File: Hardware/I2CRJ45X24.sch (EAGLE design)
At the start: 127 parts, among them IC1 MCP23017SO, IC2 MCP23017SO, IC3 MCP23017SO, IC4 MCP23017SO, IC5 MCP23017SO, IC6 MCP23017SO, J1 RJ45-X8, J2 RJ45-X8, J3 RJ45-X8, J4 I2C-BREAKOUT, J5 M01-PLAIN, J9 I2C-BREAKOUT

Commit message: Renumbered parts to optimise production.
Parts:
- removed J9: I2C-BREAKOUT, SuperHouse-Connectors:M02X3-SHROUDED
- added J6: M01-PLAIN, SuperHouse-Connectors:M01-PLAIN
- J5: value M01-PLAIN -> I2C-BREAKOUT; device SuperHouse-Connectors:M01-PLAIN -> SuperHouse-Connectors:M02X3-SHROUDED
- R100, R99: value 1K -> 4K7
- R68, R69: value 4K7 -> 1K
- renumbered LED3 to LED1, R101 to R67
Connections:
- net !INT: now also J6.1; no longer J5.1
- net !RESET: now also J5.6; no longer J9.6
- net 3D1: now also R68.2; no longer R100.2
- net 3H2: now also R69.2; no longer R99.2
- net GND: now also J5.4; no longer J9.4
- net GPB0-6: now also R68.1; no longer R100.1
- net GPB5-6: now also R69.1; no longer R99.1
- net N$1: now also R99.2; no longer R68.2
- net N$2: now also R100.2; no longer R69.2
- net SCL: now also J5.1, R99.1; no longer J9.1, R68.1
- net SDA: now also J5.2, R100.1; no longer J9.2, R69.1
- net VCC: now also J5.5; no longer J9.5
- net VIN: now also J5.3; no longer J9.3
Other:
- note added: "24-Channel I2C RJ45 Breakout"
- note added: "V2.2 (2021-04-14)"
- note removed: "24 Channel I2C RJ45 Breakout"
- note removed: "V2.2 (2021-04-08)"

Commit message: Major clean-up in preparation for recreating x8 and x16 versions based on the x24 version. Moved rear silkscreen into left third. Increased size of all data traces. Improved bottom power plane pour. Changed LED resistors to 4K7.
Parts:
- J1, J2: value RJ45-X8 -> I2C-BREAKOUT; device SuperHouse-Connectors:RJ45-X8 -> SuperHouse-Connectors:M02X3-SHROUDED
- J3: value RJ45-X8 -> M01-PLAIN; device SuperHouse-Connectors:RJ45-X8 -> SuperHouse-Connectors:M01-PLAIN
- J4, J5: value I2C-BREAKOUT -> RJ45-X8; device SuperHouse-Connectors:M02X3-SHROUDED -> SuperHouse-Connectors:RJ45-X8
- J6: value M01-PLAIN -> RJ45-X8; device SuperHouse-Connectors:M01-PLAIN -> SuperHouse-Connectors:RJ45-X8
- R39, R40: value 2K2 -> 1K
- R97, R98: value 1K -> 4K7
- renumbered SJ3 to SJ1
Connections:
- net !INT: now also J3.1; no longer J6.1
- net !RESET: now also J1.6, J2.6; no longer J4.6, J5.6
- net 1A1: now also J4.A1; no longer J1.A1
- net 1A2: now also J4.A2; no longer J1.A2
- net 1A3: now also J4.A3; no longer J1.A3
- net 1A6: now also J4.A6; no longer J1.A6
- net 1B1: now also J4.B1; no longer J1.B1
- net 1B2: now also J4.B2; no longer J1.B2
- net 1B3: now also J4.B3; no longer J1.B3
- net 1B6: now also J4.B6; no longer J1.B6
- net 1C1: now also J4.C1; no longer J1.C1
- net 1C2: now also J4.C2; no longer J1.C2
- net 1C3: now also J4.C3; no longer J1.C3
- net 1C6: now also J4.C6; no longer J1.C6
- net 1D1: now also J4.D1; no longer J1.D1
- net 1D2: now also J4.D2; no longer J1.D2
- net 1D3: now also J4.D3; no longer J1.D3
- net 1D6: now also J4.D6; no longer J1.D6
- net 1E1: now also J4.E1; no longer J1.E1
- net 1E2: now also J4.E2; no longer J1.E2
- net 1E3: now also J4.E3; no longer J1.E3
- net 1E6: now also J4.E6; no longer J1.E6
- net 1F1: now also J4.F1; no longer J1.F1
- net 1F2: now also J4.F2; no longer J1.F2
- net 1F3: now also J4.F3; no longer J1.F3
- net 1F6: now also J4.F6; no longer J1.F6
- net 1G1: now also J4.G1; no longer J1.G1
- net 1G2: now also J4.G2; no longer J1.G2
- net 1G3: now also J4.G3; no longer J1.G3
- net 1G6: now also J4.G6; no longer J1.G6
- net 1H1: now also J4.H1; no longer J1.H1
- net 1H2: now also J4.H2; no longer J1.H2
- net 1H3: now also J4.H3; no longer J1.H3
- net 1H6: now also J4.H6; no longer J1.H6
- net 2A1: now also J5.A1; no longer J2.A1
- net 2A2: now also J5.A2; no longer J2.A2
- net 2A3: now also J5.A3; no longer J2.A3
- net 2A6: now also J5.A6; no longer J2.A6
- net 2B1: now also J5.B1; no longer J2.B1
- net 2B2: now also J5.B2; no longer J2.B2
- net 2B3: now also J5.B3; no longer J2.B3
- net 2B6: now also J5.B6; no longer J2.B6
- net 2C1: now also J5.C1; no longer J2.C1
- net 2C2: now also J5.C2; no longer J2.C2
- net 2C3: now also J5.C3; no longer J2.C3
- net 2C6: now also J5.C6; no longer J2.C6
- net 2D1: now also J5.D1; no longer J2.D1
- net 2D2: now also J5.D2; no longer J2.D2
- net 2D3: now also J5.D3; no longer J2.D3
- net 2D6: now also J5.D6; no longer J2.D6
- net 2E1: now also J5.E1; no longer J2.E1
- net 2E2: now also J5.E2; no longer J2.E2
- net 2E3: now also J5.E3; no longer J2.E3
- net 2E6: now also J5.E6; no longer J2.E6
- net 2F1: now also J5.F1; no longer J2.F1
- net 2F2: now also J5.F2; no longer J2.F2
- net 2F3: now also J5.F3; no longer J2.F3
- net 2F6: now also J5.F6; no longer J2.F6
- net 2G1: now also J5.G1; no longer J2.G1
- net 2G2: now also J5.G2; no longer J2.G2
- net 2G3: now also J5.G3; no longer J2.G3
- net 2G6: now also J5.G6; no longer J2.G6
- net 2H1: now also J5.H1; no longer J2.H1
- net 2H2: now also J5.H2; no longer J2.H2
- net 2H3: now also J5.H3; no longer J2.H3
- net 2H6: now also J5.H6; no longer J2.H6
- net 3A1: now also J6.A1; no longer J3.A1
- net 3A2: now also J6.A2; no longer J3.A2
- net 3A3: now also J6.A3; no longer J3.A3
- net 3A6: now also J6.A6; no longer J3.A6
- net 3B1: now also J6.B1; no longer J3.B1
- net 3B2: now also J6.B2; no longer J3.B2
- net 3B3: now also J6.B3; no longer J3.B3
- net 3B6: now also J6.B6; no longer J3.B6
- net 3C1: now also J6.C1; no longer J3.C1
- net 3C2: now also J6.C2; no longer J3.C2
- net 3C3: now also J6.C3; no longer J3.C3
- net 3C6: now also J6.C6; no longer J3.C6
- net 3D1: now also J6.D1; no longer J3.D1
- net 3D2: now also J6.D2, R40.2; no longer J3.D2, R98.2
- net 3D3: now also J6.D3; no longer J3.D3
- net 3D6: now also J6.D6; no longer J3.D6
- net 3E1: now also J6.E1; no longer J3.E1
- net 3E2: now also J6.E2; no longer J3.E2
- net 3E3: now also J6.E3; no longer J3.E3
- net 3E6: now also J6.E6; no longer J3.E6
- net 3F1: now also J6.F1; no longer J3.F1
- net 3F2: now also J6.F2; no longer J3.F2
- net 3F3: now also J6.F3; no longer J3.F3
- net 3F6: now also J6.F6; no longer J3.F6
- net 3G1: now also J6.G1; no longer J3.G1
- net 3G2: now also J6.G2; no longer J3.G2
- net 3G3: now also J6.G3; no longer J3.G3
- net 3G6: now also J6.G6; no longer J3.G6
- net 3H1: now also J6.H1; no longer J3.H1
- net 3H2: now also J6.H2; no longer J3.H2
- net 3H3: now also J6.H3, R39.2; no longer J3.H3, R97.2
- net 3H6: now also J6.H6; no longer J3.H6
- net GND: now also J1.4, J2.4, J4.A7, J4.A8, J4.B7, J4.B8, J4.C7, J4.C8, J4.D7, J4.D8, J4.E7, J4.E8, J4.F7, J4.F8, J4.G7, J4.G8, J4.GND0, J4.GND1, J4.GND2, J4.GND3, J4.GND4, J4.GND5, J4.H7, J4.H8, J5.A7, J5.A8, J5.B7, J5.B8, J5.C7, J5.C8, J5.D7, J5.D8, J5.E7, J5.E8, J5.F7, J5.F8, J5.G7, J5.G8, J5.GND0, J5.GND1, J5.GND2, J5.GND3, J5.GND4, J5.GND5, J5.H7, J5.H8, J6.A7, J6.A8, J6.B7, J6.B8, J6.C7, J6.C8, J6.D7, J6.D8, J6.E7, J6.E8, J6.F7, J6.F8, J6.G7, J6.G8, J6.GND0, J6.GND1, J6.GND2, J6.GND3, J6.GND4, J6.GND5, J6.H7, J6.H8; no longer J1.A7, J1.A8, J1.B7, J1.B8, J1.C7, J1.C8, J1.D7, J1.D8, J1.E7, J1.E8, J1.F7, J1.F8, J1.G7, J1.G8, J1.GND0, J1.GND1, J1.GND2, J1.GND3, J1.GND4, J1.GND5, J1.H7, J1.H8, J2.A7, J2.A8, J2.B7, J2.B8, J2.C7, J2.C8, J2.D7, J2.D8, J2.E7, J2.E8, J2.F7, J2.F8, J2.G7, J2.G8, J2.GND0, J2.GND1, J2.GND2, J2.GND3, J2.GND4, J2.GND5, J2.H7, J2.H8, J3.A7, J3.A8, J3.B7, J3.B8, J3.C7, J3.C8, J3.D7, J3.D8, J3.E7, J3.E8, J3.F7, J3.F8, J3.G7, J3.G8, J3.GND0, J3.GND1, J3.GND2, J3.GND3, J3.GND4, J3.GND5, J3.H7, J3.H8, J4.4, J5.4
- net GPB1-6: now also R40.1; no longer R98.1
- net GPB6-6: now also R39.1; no longer R97.1
- net N$7: now also R97.1; no longer R39.1
- net N$8: now also R98.1; no longer R40.1
- net SCL: now also J1.1, J2.1; no longer J4.1, J5.1
- net SDA: now also J1.2, J2.2; no longer J4.2, J5.2
- net VCC: now also J1.5, J2.5, R97.2; no longer J4.5, J5.5, R39.2
- net VIN: now also J1.3, J2.3, J4.A4, J4.A5, J4.B4, J4.B5, J4.C4, J4.C5, J4.D4, J4.D5, J4.E4, J4.E5, J4.F4, J4.F5, J4.G4, J4.G5, J4.H4, J4.H5, J5.A4, J5.A5, J5.B4, J5.B5, J5.C4, J5.C5, J5.D4, J5.D5, J5.E4, J5.E5, J5.F4, J5.F5, J5.G4, J5.G5, J5.H4, J5.H5, J6.A4, J6.A5, J6.B4, J6.B5, J6.C4, J6.C5, J6.D4, J6.D5, J6.E4, J6.E5, J6.F4, J6.F5, J6.G4, J6.G5, J6.H4, J6.H5, R98.2; no longer J1.A4, J1.A5, J1.B4, J1.B5, J1.C4, J1.C5, J1.D4, J1.D5, J1.E4, J1.E5, J1.F4, J1.F5, J1.G4, J1.G5, J1.H4, J1.H5, J2.A4, J2.A5, J2.B4, J2.B5, J2.C4, J2.C5, J2.D4, J2.D5, J2.E4, J2.E5, J2.F4, J2.F5, J2.G4, J2.G5, J2.H4, J2.H5, J3.A4, J3.A5, J3.B4, J3.B5, J3.C4, J3.C5, J3.D4, J3.D5, J3.E4, J3.E5, J3.F4, J3.F5, J3.G4, J3.G5, J3.H4, J3.H5, J4.3, J5.3, R40.2
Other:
- note added: "Power"
- note removed: "External Power"
- note removed: "Power LEDs"
- moved on the sheet: C7, C8, LED1

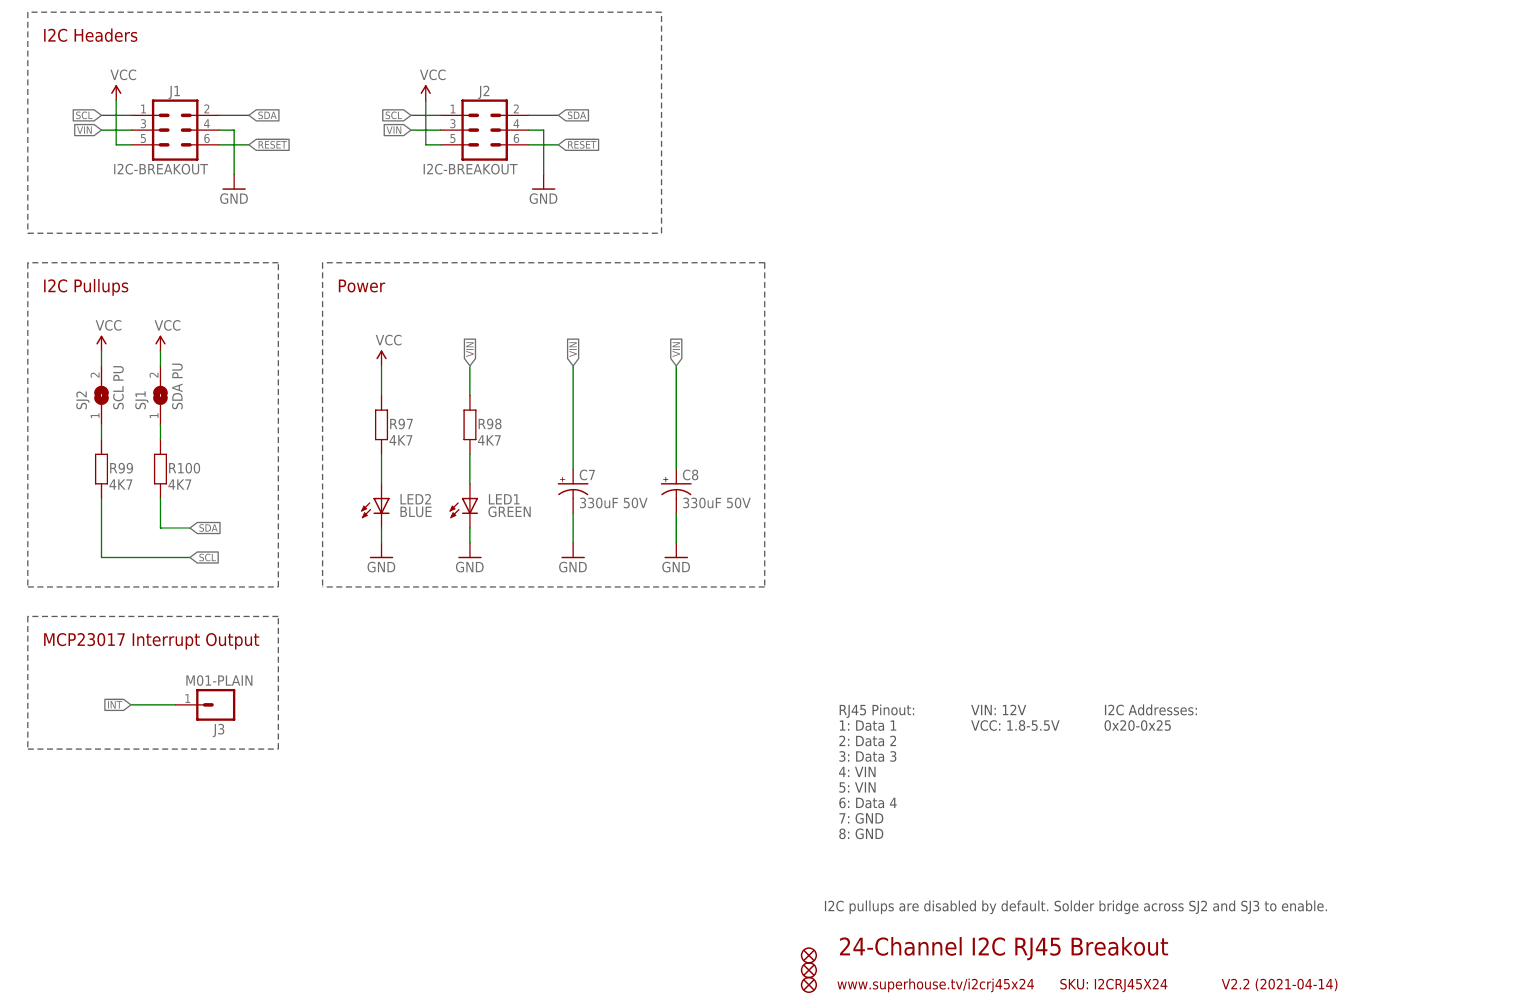
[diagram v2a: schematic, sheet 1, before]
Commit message: Added weak pull-up on RESET line.
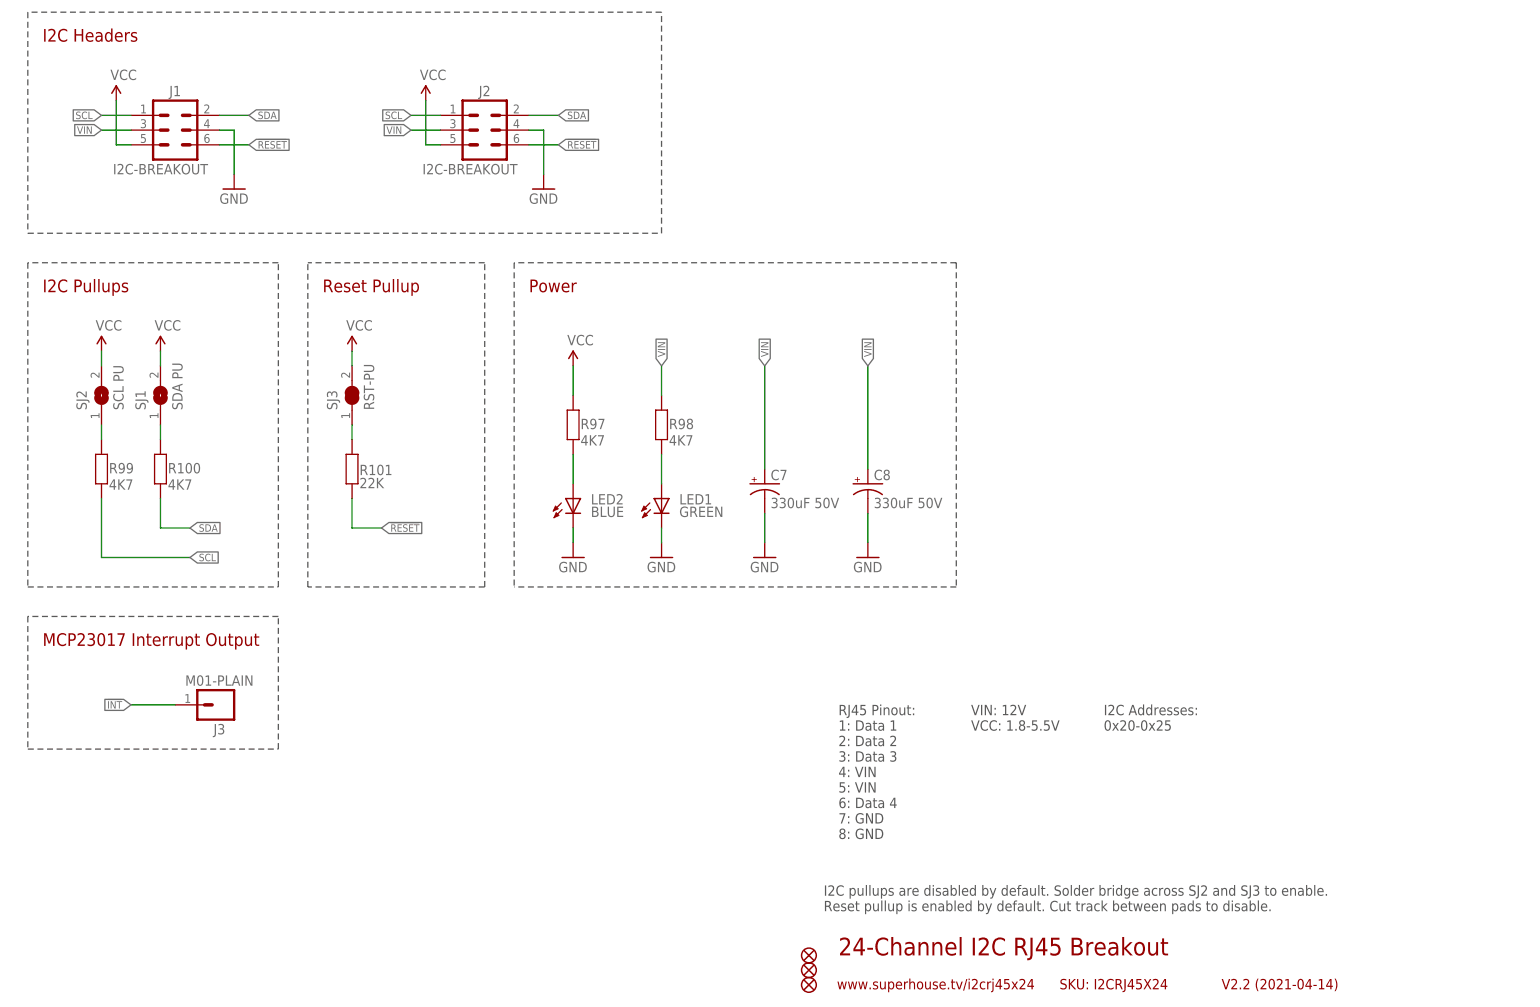
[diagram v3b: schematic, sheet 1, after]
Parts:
- added R101: 22K, SuperHouse-DiscreteSemi:RESISTOR0603
- added SJ3: RST-PU, SuperHouse-Jumpers:SJC-NORMAL
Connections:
- new net N$3: R101.2, SJ3.1
- net !RESET: now also R101.1
- net VCC: now also SJ3.2
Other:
- note added: "I2C pullups are disabled by default. Solder bridge across SJ2 and SJ3 to enable. Reset pullup is enabled by default. Cut track between pads to disable."
- note added: "Reset Pullup"
- note removed: "I2C pullups are disabled by default. Solder bridge across SJ2 and SJ3 to enable."
- moved on the sheet: C7, C8, LED1, LED2, R97, R98

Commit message: Bumped version to v3.0 for release.
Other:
- note added: "V3.0 (2021-04-15)"
- note removed: "V2.2 (2021-04-14)"
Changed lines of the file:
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@@
 <frame x1="0" y1="0" x2="248.92" y2="185.42" columns="8" rows="5" layer="94"/>
 <text x="149.86" y="12.7" size="3.048" layer="94">24-Channel I2C RJ45 Breakout</text>
-<text x="215.9" y="6.858" size="1.778" layer="94">V2.2 (2021-04-14)</text>
+<text x="215.9" y="6.858" size="1.778" layer="94">V3.0 (2021-04-15)</text>
 <text x="149.606" y="6.858" size="1.778" layer="94">www.superhouse.tv/i2crj45x24</text>
 <text x="187.96" y="6.858" size="1.778" layer="94">SKU: I2CRJ45X24</text>
